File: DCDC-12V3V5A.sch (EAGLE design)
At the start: 36 parts, among them CN2 2828XX-2282834-2, CN3 2828XX-2282834-2, Q10 NMOSFET, Q9 NMOSFET, U1 LM3150MHX/NOPB

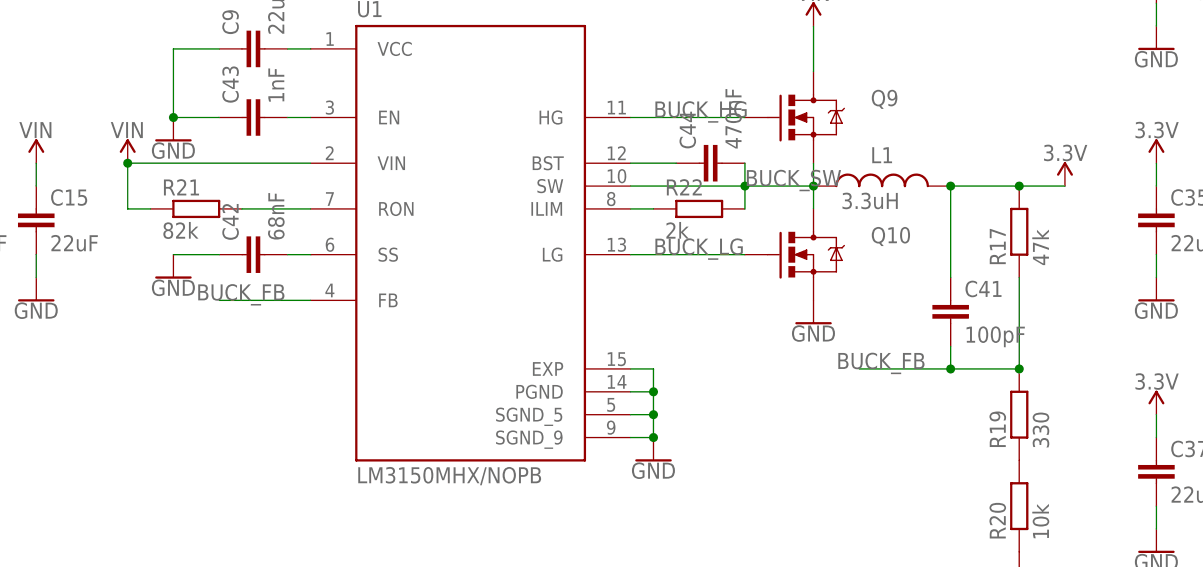
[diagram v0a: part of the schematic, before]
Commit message: Fixed few values on 3.3V schematics. Generated CAM files.
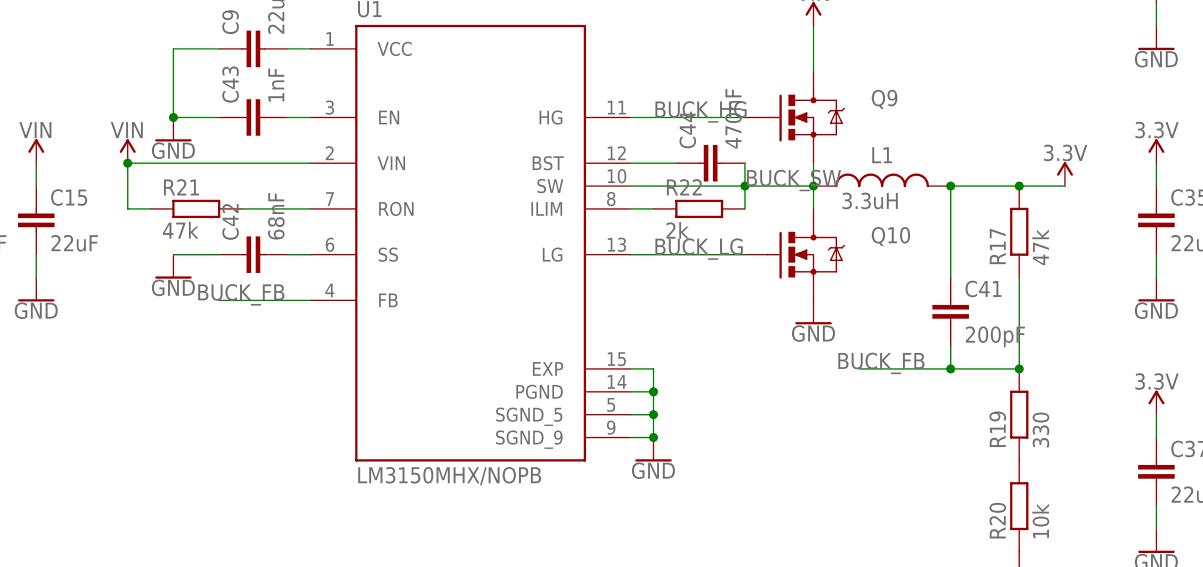
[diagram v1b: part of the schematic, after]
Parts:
- C41: value 100pF -> 200pF
- R21: value 82k -> 47k
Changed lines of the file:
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@@
 <part name="R20" library="rcl" library_urn="urn:adsk.eagle:library:334" deviceset="R-EU_" device="R0603" package3d_urn="urn:adsk.eagle:package:23555/3" value="10k"/>
 <part name="GND53" library="SparkFun-PowerSymbols" library_urn="urn:adsk.eagle:library:530" deviceset="GND" device=""/>
-<part name="C41" library="rcl" library_urn="urn:adsk.eagle:library:334" deviceset="C-EU" device="C0603K" package3d_urn="urn:adsk.eagle:package:23680/2" value="100pF"/>
+<part name="C41" library="rcl" library_urn="urn:adsk.eagle:library:334" deviceset="C-EU" device="C0603K" package3d_urn="urn:adsk.eagle:package:23680/2" value="200pF"/>
 <part name="C42" library="rcl" library_urn="urn:adsk.eagle:library:334" deviceset="C-EU" device="C0603K" package3d_urn="urn:adsk.eagle:package:23680/2" value="68nF"/>
 <part name="GND54" library="SparkFun-PowerSymbols" library_urn="urn:adsk.eagle:library:530" deviceset="GND" device=""/>
 <part name="C43" library="rcl" library_urn="urn:adsk.eagle:library:334" deviceset="C-EU" device="C0603K" package3d_urn="urn:adsk.eagle:package:23680/2" value="1nF"/>
 <part name="GND55" library="SparkFun-PowerSymbols" library_urn="urn:adsk.eagle:library:530" deviceset="GND" device=""/>
-<part name="R21" library="rcl" library_urn="urn:adsk.eagle:library:334" deviceset="R-EU_" device="R0603" package3d_urn="urn:adsk.eagle:package:23555/3" value="82k"/>
+<part name="R21" library="rcl" library_urn="urn:adsk.eagle:library:334" deviceset="R-EU_" device="R0603" package3d_urn="urn:adsk.eagle:package:23555/3" value="47k"/>
 <part name="R22" library="rcl" library_urn="urn:adsk.eagle:library:334" deviceset="R-EU_" device="R0603" package3d_urn="urn:adsk.eagle:package:23555/3" value="2k"/>
 <part name="C44" library="rcl" library_urn="urn:adsk.eagle:library:334" deviceset="C-EU" device="C0603K" package3d_urn="urn:adsk.eagle:package:23680/2" value="470nF"/>

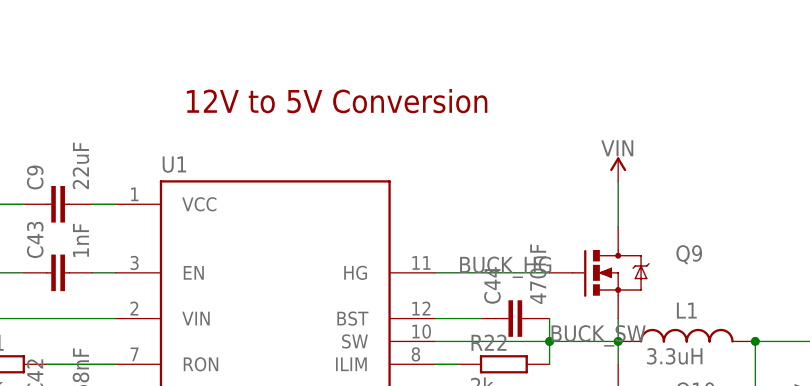
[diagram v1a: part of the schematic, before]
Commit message: Text fixed.
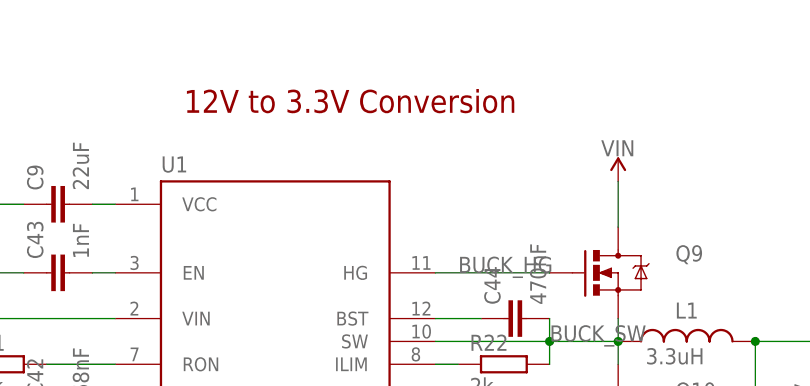
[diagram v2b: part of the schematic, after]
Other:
- note added: "12V to 3.3V Conversion"
- note removed: "12V to 5V Conversion"
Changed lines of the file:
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@@
 <text x="165.1" y="25.4" size="2.54" layer="94">DC-DC Buck Converter with fixed output 3.3V
 (c) Andriy Golovnya</text>
-<text x="106.68" y="137.16" size="2.54" layer="94">12V to 5V Conversion</text>
+<text x="106.68" y="137.16" size="2.54" layer="94">12V to 3.3V Conversion</text>
 </plain>
 <instances>

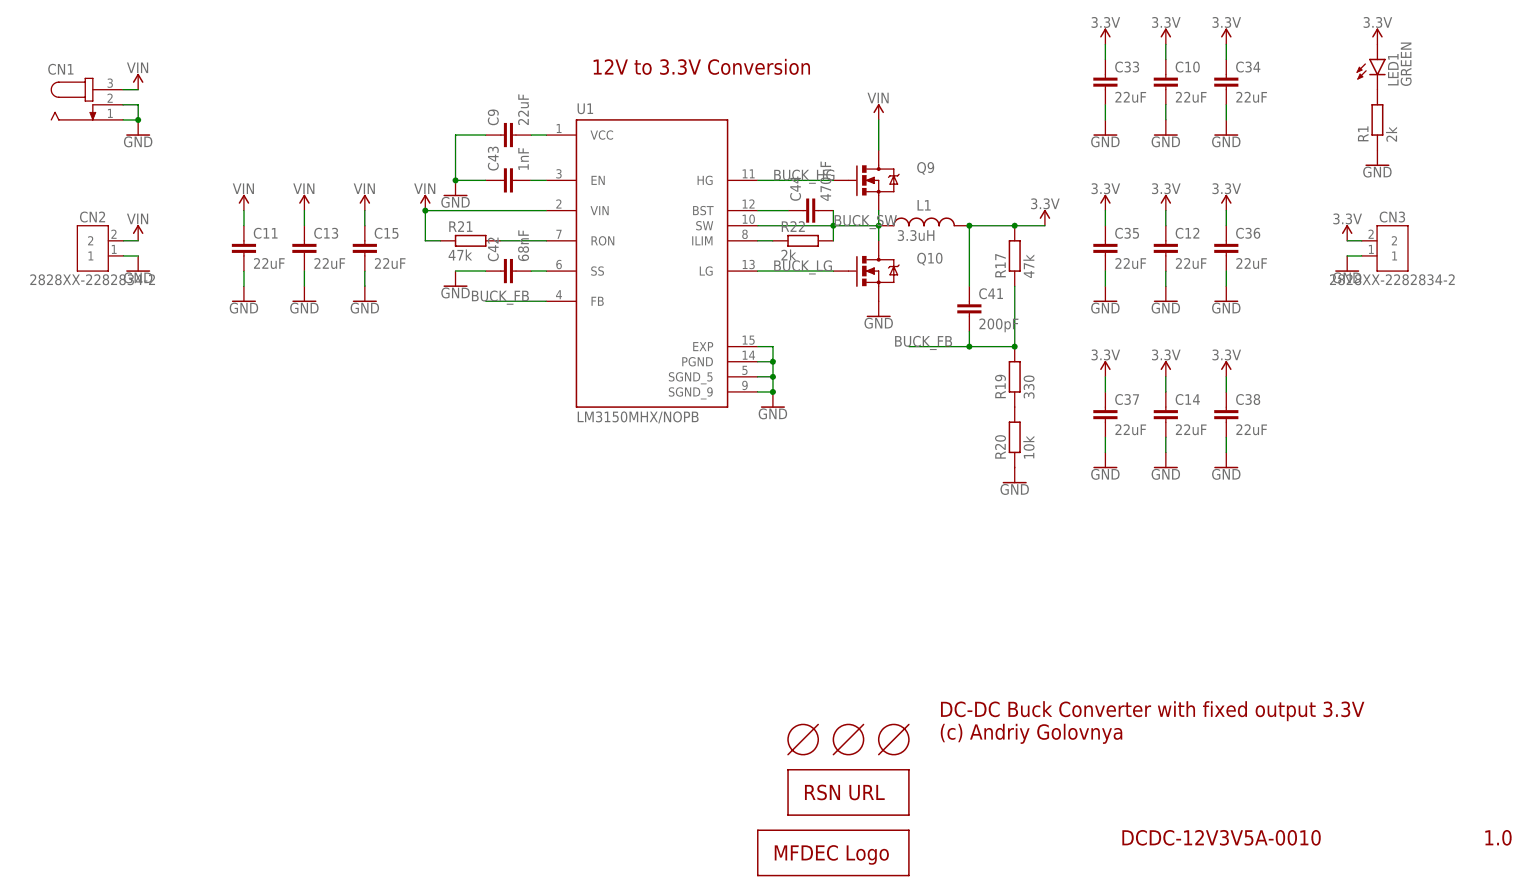
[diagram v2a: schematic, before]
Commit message: Improved layout of DC-DC board. Rotated input terminal. Generated CAM files. Generated BoM and PnP files. Generated PNG preview. Generated PDF schematics.
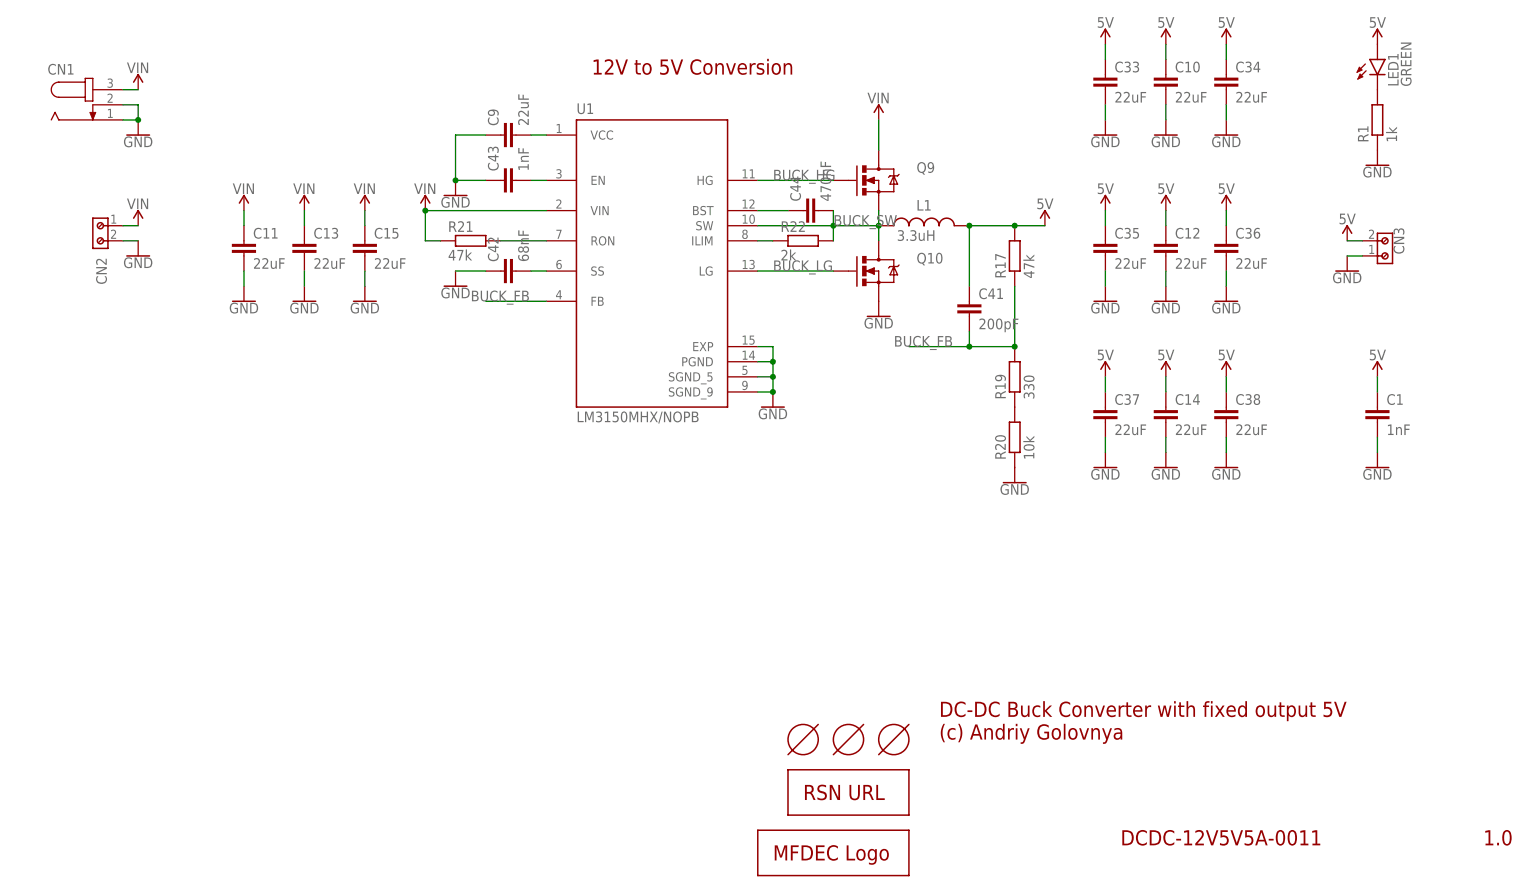
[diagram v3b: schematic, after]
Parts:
- added C1: 1nF, rcl:C-EUC0603K
- CN2, CN3: value 2828XX-2282834-2 -> (none); device Connector:2828XX-2282834-2 -> Wurth_Connectors_WR-TBL Rising Cage Clamp:691213510002
- R1: value 2k -> 1k
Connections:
- net N$16 renamed BUCK_SS
- net N$18 renamed BUCK_EN
- net N$19 renamed BUCK_VCC
- net N$21 renamed BUCK_RON
- net N$23 renamed BUCK_BST
- net N$8 renamed BUCK_ILIM
- removed net 3.3V: C10.1, C12.1, C14.1, C33.1, C34.1, C35.1, C36.1, C37.1, C38.1, C41.1, CN3.2, L1.2, LED1.A, R17.2
- new net 5V: C1.1, C10.1, C12.1, C14.1, C33.1, C34.1, C35.1, C36.1, C37.1, C38.1, C41.1, CN3.2, L1.2, LED1.A, R17.2
- net GND: now also C1.2, CN2.2; no longer CN2.1
- net VIN: now also CN2.1; no longer CN2.2
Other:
- note added: "12V to 5V Conversion"
- note added: "DC-DC Buck Converter with fixed output 5V (c) Andriy Golovnya"
- note added: "DCDC-12V5V5A-0011"
- note removed: "12V to 3.3V Conversion"
- note removed: "DC-DC Buck Converter with fixed output 3.3V (c) Andriy Golovnya"
- note removed: "DCDC-12V3V5A-0010"
